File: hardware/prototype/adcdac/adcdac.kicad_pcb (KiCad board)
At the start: 2 copper layers, 65 parts, among them IC1 ADP3335, IC2 AD8138, IC3 AD8138, IC4 ADP3335, IC5 AD9744, IC6 ADP3335, IC7 ADP3335, IC8 AD8041, IC9 AD9218, J1 FPGA_GPIO0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

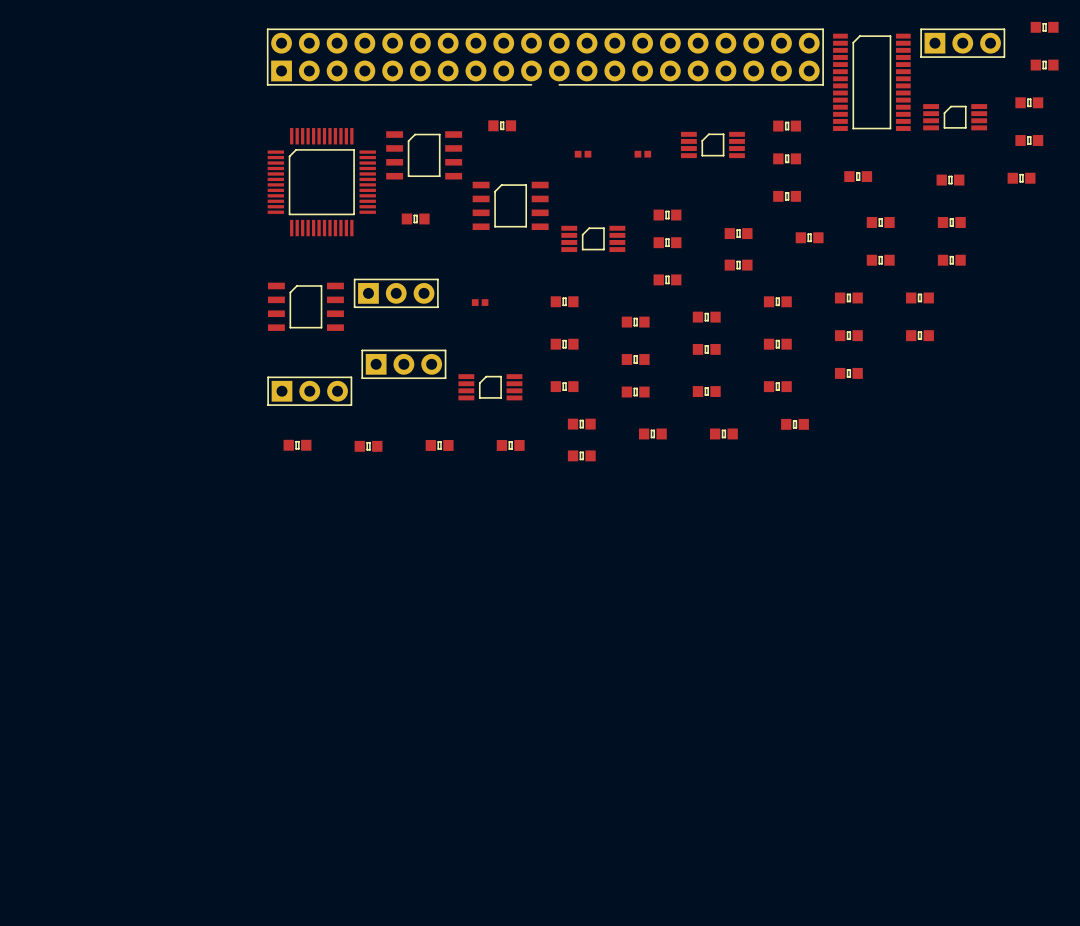
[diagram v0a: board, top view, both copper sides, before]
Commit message: finish routing, order r1 boards
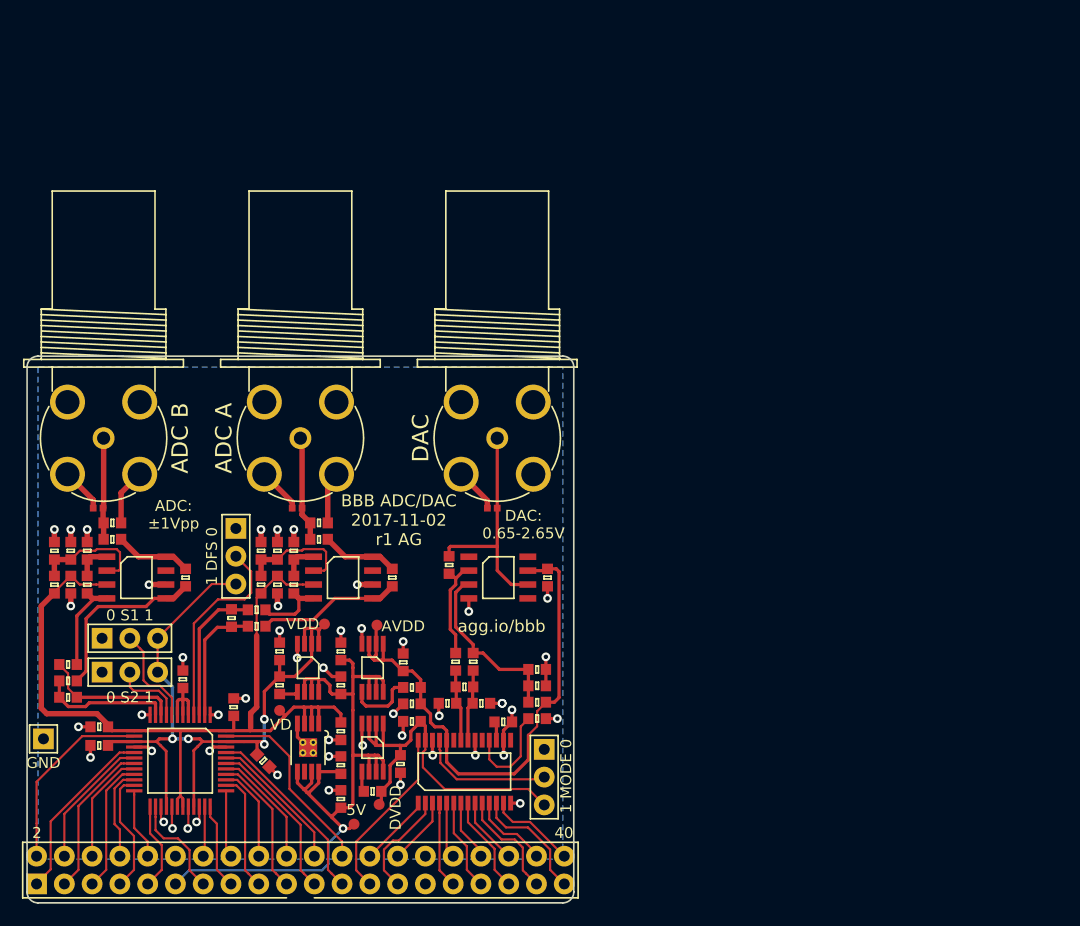
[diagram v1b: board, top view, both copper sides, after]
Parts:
- added C23: 100n, agg:0603, F.Cu at (79.0, 123.9)
- added C24: 100n, agg:0603, F.Cu at (81.6, 138.6)
- added C25: 100n, agg:0603, F.Cu at (93.9, 135.1)
- added C26: 100n, agg:0603, F.Cu at (81.6, 136.9)
- added C27: 100n, agg:0603, F.Cu at (96.6, 140.0)
- added C28: 100n, agg:0603, F.Cu at (121.7, 131.7)
- added J6: GND, agg:SIL-254P-01, F.Cu at (76.5, 138.0)
- added P1: COAX, agg:BNC_PCB_RA_5-1634556-0, F.Cu at (100.0, 110.5)
- added P2: COAX, agg:BNC_PCB_RA_5-1634556-0, F.Cu at (82.0, 110.5)
- added P3: COAX, agg:BNC_PCB_RA_5-1634556-0, F.Cu at (118.0, 110.5)
- added TP1: TESTPAD, agg:TESTPAD, F.Cu at (107.0, 127.6)
- added TP2: TESTPAD, agg:TESTPAD, F.Cu at (104.9, 145.8)
- added TP3: TESTPAD, agg:TESTPAD, F.Cu at (107.2, 144.0)
- added TP4: TESTPAD, agg:TESTPAD, F.Cu at (102.2, 127.5)
- added TP5: TESTPAD, agg:TESTPAD, F.Cu at (98.1, 135.4)
- C10, C12, C15: value C -> 15p
- C18: value 1n -> 100n
- IC7: value ADP3335 -> ADP124; footprint agg:MSOP-8 -> agg:MSOP-8-EP-AD
- R23, R24: value 10k -> 1k
- R3, R7: value 10k -> 5k
- moved R18 97.9 mm to (78.8, 131.2)
- moved J3 95.5 mm to (84.4, 131.9)
- moved C13 88.1 mm to (103.7, 133.1), turned to 90 degrees
- moved R13 86.9 mm to (89.5, 123.2), turned to 270 degrees
- moved R12 80.4 mm to (99.4, 123.9), turned to 270 degrees
- moved J1 77.7 mm to (100.0, 150.0)
- moved R14 76.5 mm to (80.5, 123.9), turned to 270 degrees
- moved R25 75.6 mm to (115.8, 130.9), turned to 270 degrees
- moved R10 73.4 mm to (80.5, 120.8), turned to 270 degrees
- moved IC1 73.3 mm to (106.6, 131.5), turned to 270 degrees
- moved IC5 73.2 mm to (115.0, 141.0), turned to 90 degrees
- moved C4 73.1 mm to (79.0, 120.8), turned to 90 degrees
- moved R16 72.8 mm to (96.0, 126.2)
- moved C6 68.7 mm to (110.2, 134.8), turned to 180 degrees
- moved C20 67.8 mm to (103.7, 137.3), turned to 270 degrees
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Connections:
- C18 pad 1: Net-(C18-Pad1) -> /ADC_VD
- C18 pad 2: /ADC_VD -> GND
- IC5 pad 1: /GPIO0_32 -> /GPIO0_21
- IC5 pad 10: /GPIO0_23 -> /GPIO0_30
- IC5 pad 11: /GPIO0_22 -> /GPIO0_31
- IC5 pad 12: /GPIO0_21 -> /GPIO0_32
- IC5 pad 13: /GPIO0_20 -> /GPIO0_33
- IC5 pad 14: Net-(IC5-Pad14) -> GND
- IC5 pad 2: /GPIO0_31 -> /GPIO0_22
- IC5 pad 28: /GPIO0_33 -> /GPIO0_20
- IC5 pad 3: /GPIO0_30 -> /GPIO0_23
- IC5 pad 4: /GPIO0_29 -> /GPIO0_24
- IC5 pad 5: /GPIO0_28 -> /GPIO0_25
- IC5 pad 6: /GPIO0_27 -> /GPIO0_26
- IC5 pad 7: /GPIO0_26 -> /GPIO0_27
- IC5 pad 8: /GPIO0_25 -> /GPIO0_28
- IC5 pad 9: /GPIO0_24 -> /GPIO0_29
- IC7 pad 5: Net-(C18-Pad1) -> 5v
- IC7 pad 6: 5v -> Net-(IC7-Pad6)
- IC9 pad 14: /GPIO0_09 -> /GPIO0_00
- IC9 pad 17: /GPIO0_19 -> /GPIO0_IN0
- IC9 pad 18: /GPIO0_18 -> /GPIO0_01
- IC9 pad 19: /GPIO0_17 -> /GPIO0_IN1
- IC9 pad 20: /GPIO0_16 -> /GPIO0_03
- IC9 pad 21: /GPIO0_15 -> /GPIO0_02
- IC9 pad 22: /GPIO0_14 -> /GPIO0_05
- IC9 pad 23: /GPIO0_13 -> /GPIO0_04
- IC9 pad 24: /GPIO0_12 -> /GPIO0_07
- IC9 pad 25: /GPIO0_11 -> /GPIO0_06
- IC9 pad 26: /GPIO0_10 -> /GPIO0_08
- IC9 pad 35: /GPIO0_IN0 -> /GPIO0_09
- IC9 pad 36: /GPIO0_IN1 -> /GPIO0_10
- IC9 pad 37: /GPIO0_00 -> /GPIO0_11
- IC9 pad 38: /GPIO0_01 -> /GPIO0_12
- IC9 pad 39: /GPIO0_02 -> /GPIO0_13
- IC9 pad 40: /GPIO0_03 -> /GPIO0_14
- IC9 pad 41: /GPIO0_04 -> /GPIO0_15
- IC9 pad 42: /GPIO0_05 -> /GPIO0_16
- IC9 pad 43: /GPIO0_06 -> /GPIO0_17
- IC9 pad 44: /GPIO0_07 -> /GPIO0_18
- IC9 pad 47: /GPIO0_08 -> /GPIO0_19
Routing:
- net GND: track 0.00 -> 87.3 mm, vias 0 -> 48
- net /ADC_VD: track 0.00 -> 81.3 mm
- net 5v: track 0.00 -> 72.4 mm, vias 0 -> 1
- net /ADC_VDD: track 0.00 -> 67.0 mm, vias 0 -> 4
- net /DAC_AVDD: track 0.00 -> 50.7 mm
- net /DAC_DVDD: track 0.00 -> 35.0 mm
- net Net-(D3-Pad1): track 0.00 -> 21.1 mm
- net Net-(IC9-Pad4): track 0.00 -> 18.7 mm
- net /GPIO0_19: track 0.00 -> 17.7 mm
- net /GPIO0_00: track 0.00 -> 17.5 mm
- net /GPIO0_18: track 0.00 -> 17.2 mm
- net Net-(C28-Pad1): track 0.00 -> 17.0 mm
- net /GPIO0_IN0: track 0.00 -> 16.6 mm
- net Net-(IC3-Pad5): track 0.00 -> 16.4 mm
- net /GPIO0_20: track 0.00 -> 16.0 mm
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- added copper zone on B.Cu, net GND
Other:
- board outline added: 50 x 50 mm
- net class Default: clearance 0.2 -> 0.195; trace_width 0.25 -> 0.2
- rule pad_to_mask_clearance: 0.2 -> 0
- rule trace_clearance: 0.2 -> 0.195
- rule via_min_size: 0.4 -> 0.6
- board text added: "0 S1 1"
- board text added: "0 S2 1"
- board text added: "1 DFS 0"
- board text added: "1 MODE 0"
- board text added: "2"
- board text added: "40"
- board text added: "5V"
- board text added: "ADC A"
- board text added: "ADC B"
- board text added: "ADC: ±1Vpp"
- board text added: "AVDD"
- board text added: "BBB ADC/DAC 2017-11-02 r1 AG"
- board text added: "DAC"
- board text added: "DAC: 0.65-2.65V"
- board text added: "DVDD"
- board text added: "GND"
- board text added: "VD"
- board text added: "VDD"
- board text added: "agg.io/bbb"
